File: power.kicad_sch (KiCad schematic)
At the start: 16 parts, among them IC1 MP2456GJ-Z, IC2 AP2112K-3.3TRG1

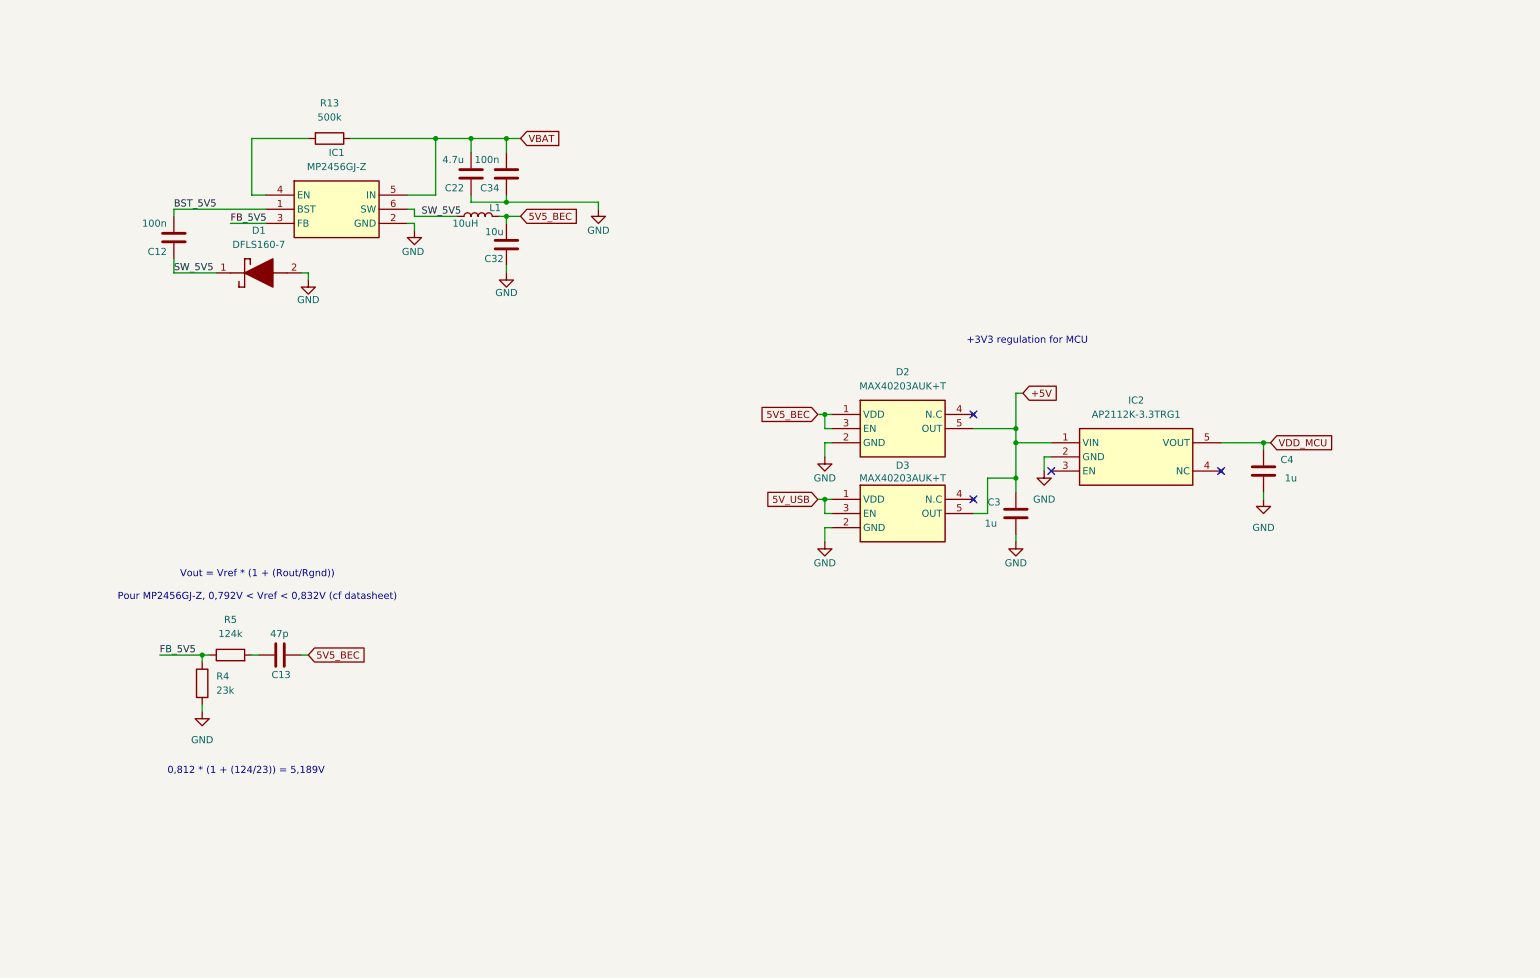
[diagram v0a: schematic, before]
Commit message: finished one full channel, still to duplicate this for 4 channels esc
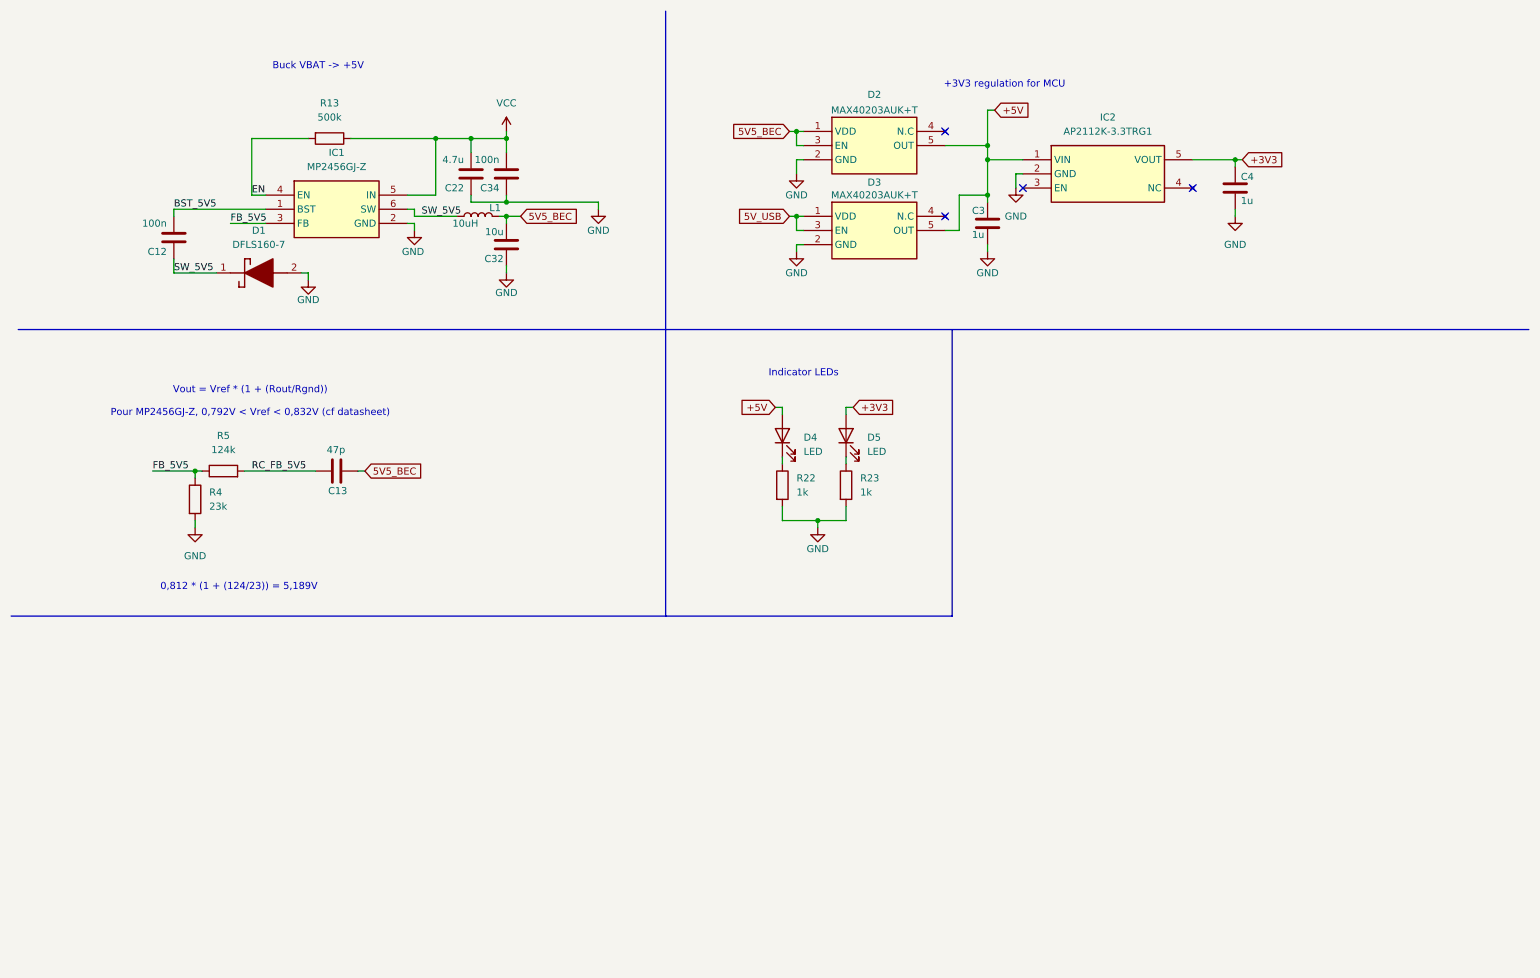
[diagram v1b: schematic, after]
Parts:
- added D4, D5: LED, symbol Device:LED
- added R22, R23: 1k, Resistor_SMD:R_0402_1005Metric, symbol Device:R
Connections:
- net +5V: now also D4.2 (A)
- net GND: now also R22.2, R23.2
- net EN: now reaches IC1.4 (EN), R13.2
- net RC_FB_5V5: now reaches C13.2, R5.2
- net VBAT renamed VCC
- net VDD_MCU renamed +3V3
- net +3V3: now also D5.2 (A)
- new net: D4.1 (K), R22.1
- new net: D5.1 (K), R23.1
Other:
- note added: "Buck VBAT -> +5V"
- note added: "Indicator LEDs"
- moved on the sheet: C13, C3, C4, D2, D3, IC2, R4, R5

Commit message: update schematic
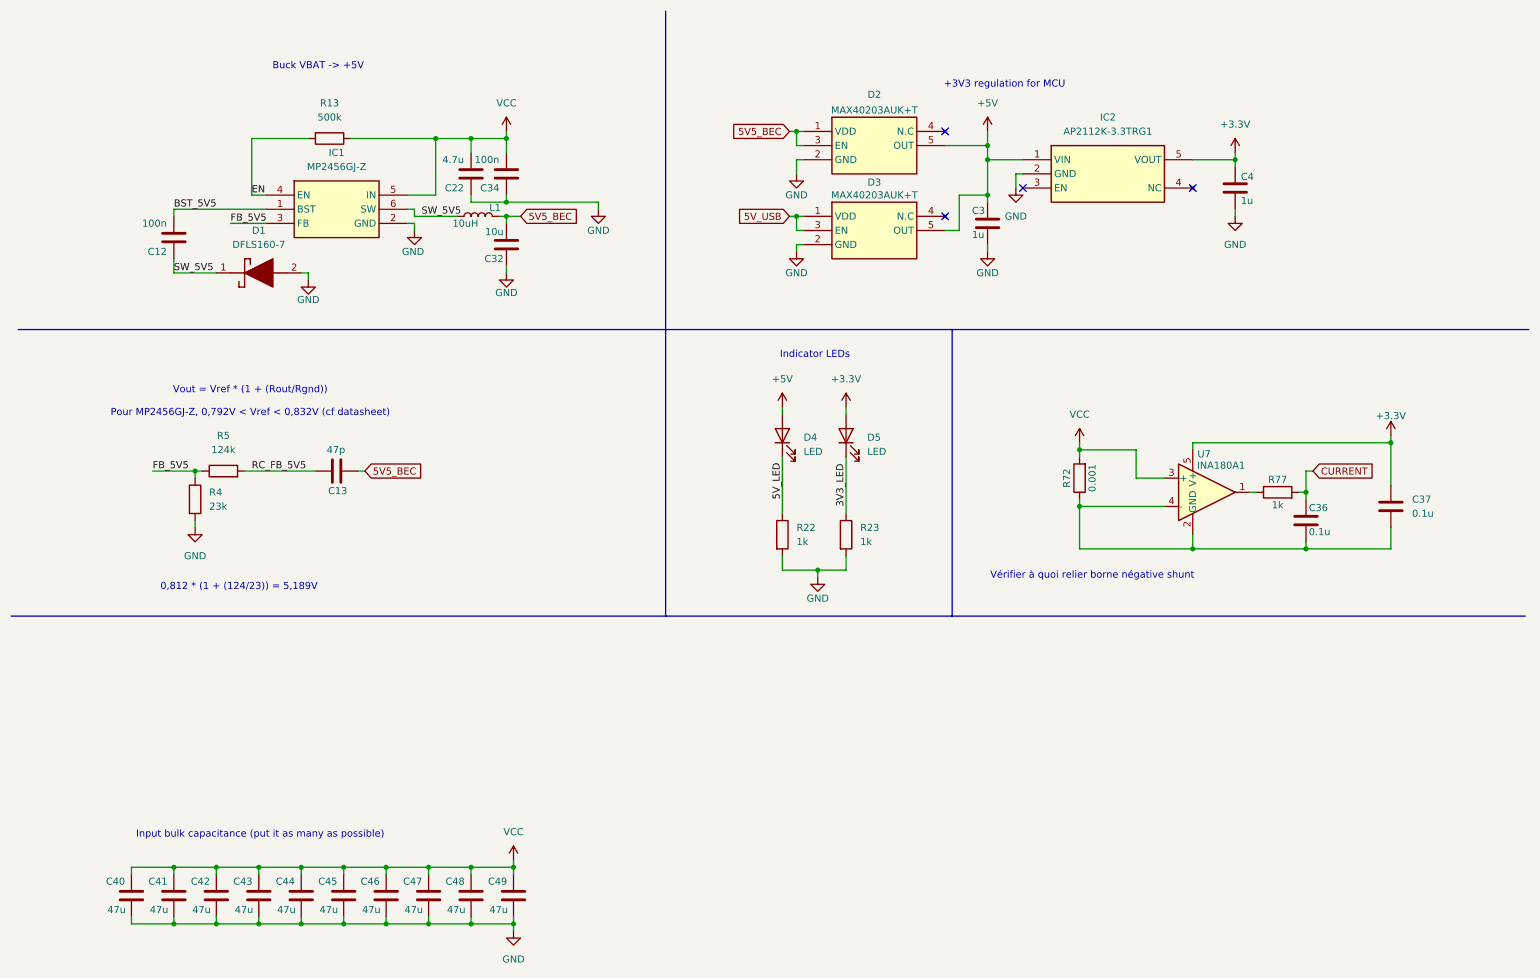
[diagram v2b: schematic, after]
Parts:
- added C36, C37: 0.1u, symbol Device:C
- added C40, C41, C42, C43, C44, C45, C46, C47, C48, C49: 47u, Capacitor_SMD:C_0402_1005Metric, symbol Device:C
- added R72: 0.001, symbol Device:R
- added R77: 1k, symbol Device:R
- added U7: INA180A1, Package_TO_SOT_SMD:SOT-23-5, symbol Amplifier_Current:INA180A1
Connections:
- net GND: now also C40.2, C41.2, C42.2, C43.2, C44.2, C45.2, C46.2, C47.2, C48.2, C49.2
- net VCC: now also C40.1, C41.1, C42.1, C43.1, C44.1, C45.1, C46.1, C47.1, C48.1, C49.1, R72.2, U7.3 (+)
- net 5V_LED: now reaches D4.1 (K), R22.1
- net 3V3_LED: now reaches D5.1 (K), R23.1
- net +3V3 renamed +3.3V
- net +3.3V: now also C37.1, U7.5 (V+)
- new net: R77.1, U7.1
- new net: C36.2, C37.2, R72.1, U7.2 (GND), U7.4 (-)
- new net CURRENT: C36.1, R77.2
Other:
- note added: "Input bulk capacitance (put it as many as possible)"
- note added: "Vérifier à quoi relier borne négative shunt"
- moved on the sheet: R22, R23

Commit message: affected footprints
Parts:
- C12, C34: value 100n -> 0.1u
- C36, C37: footprint (none) -> Capacitor_SMD:C_0402_1005Metric
- C40, C41, C42, C43, C44, C45, C46, C47, C48, C49: footprint Capacitor_SMD:C_0402_1005Metric -> Capacitor_SMD:C_0805_2012Metric
- D4, D5: footprint (none) -> ESCs:LED_L135-G525003500000
- R72: footprint (none) -> Resistor_SMD:R_2512_6332Metric
- R77: footprint (none) -> Resistor_SMD:R_0402_1005Metric
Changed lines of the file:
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@@
 			)
 		)
-		(property "Footprint" ""
+		(property "Footprint" "Resistor_SMD:R_0402_1005Metric"
 			(at 238.76 100.838 90)
 			(effects
@@
 			)
 		)
-		(property "Value" "100n"
+		(property "Value" "0.1u"
 			(at 99.06 39.37 0)
 			(effects
@@
 			)
 		)
-		(property "Footprint" ""
+		(property "Footprint" "Capacitor_SMD:C_0402_1005Metric"
 			(at 244.8052 107.95 0)
 			(effects
@@
 			)
 		)
-		(property "Footprint" "Capacitor_SMD:C_0402_1005Metric"
+		(property "Footprint" "Capacitor_SMD:C_0805_2012Metric"
 			(at 41.6052 175.26 0)
 			(effects
@@
 			)
 		)
-		(property "Footprint" "Capacitor_SMD:C_0402_1005Metric"
+		(property "Footprint" "Capacitor_SMD:C_0805_2012Metric"
 			(at 94.9452 175.26 0)
 			(effects
@@
 			)
 		)
-		(property "Footprint" "Capacitor_SMD:C_0402_1005Metric"
+		(property "Footprint" "Capacitor_SMD:C_0805_2012Metric"
 			(at 49.2252 175.26 0)
 			(effects
@@
 			)
 		)
-		(property "Value" "100n"
+		(property "Value" "0.1u"
 			(at 39.37 50.8 0)
 			(effects
@@
 			)
 		)
-		(property "Footprint" "Capacitor_SMD:C_0402_1005Metric"
+		(property "Footprint" "Capacitor_SMD:C_0805_2012Metric"
 			(at 56.8452 175.26 0)
 			(effects
@@
 			)
 		)
-		(property "Footprint" ""
+		(property "Footprint" "Resistor_SMD:R_2512_6332Metric"
 			(at 204.978 96.52 90)
 			(effects
@@
 			)
 		)
-		(property "Footprint" ""
+		(property "Footprint" "Capacitor_SMD:C_0402_1005Metric"
 			(at 260.0452 105.41 0)
 			(effects
@@
 			)
 		)
-		(property "Footprint" "Capacitor_SMD:C_0402_1005Metric"
+		(property "Footprint" "Capacitor_SMD:C_0805_2012Metric"
 			(at 87.3252 175.26 0)
 			(effects
@@
 			)
 		)
-		(property "Footprint" "Capacitor_SMD:C_0402_1005Metric"
+		(property "Footprint" "Capacitor_SMD:C_0805_2012Metric"
 			(at 79.7052 175.26 0)
 			(effects
@@
 			)
 		)
-		(property "Footprint" ""
+		(property "Footprint" "ESCs:LED_L135-G525003500000"
 			(at 161.29 88.9 0)
 			(effects
@@
 			)
 		)
-		(property "Footprint" "Capacitor_SMD:C_0402_1005Metric"
+		(property "Footprint" "Capacitor_SMD:C_0805_2012Metric"
 			(at 33.9852 175.26 0)
 			(effects
@@
 			)
 		)
-		(property "Footprint" ""
+		(property "Footprint" "ESCs:LED_L135-G525003500000"
 			(at 149.86 88.9 0)
 			(effects
@@
 			)
 		)
-		(property "Footprint" "Capacitor_SMD:C_0402_1005Metric"
+		(property "Footprint" "Capacitor_SMD:C_0805_2012Metric"
 			(at 64.4652 175.26 0)
 			(effects
@@
 			)
 		)
-		(property "Footprint" "Capacitor_SMD:C_0402_1005Metric"
+		(property "Footprint" "Capacitor_SMD:C_0805_2012Metric"
 			(at 102.5652 175.26 0)
 			(effects
@@
 			)
 		)
-		(property "Footprint" "Capacitor_SMD:C_0402_1005Metric"
+		(property "Footprint" "Capacitor_SMD:C_0805_2012Metric"
 			(at 72.0852 175.26 0)
 			(effects
